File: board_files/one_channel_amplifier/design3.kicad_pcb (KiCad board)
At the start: 2 copper layers, 50.8 x 50.8 mm, 27 parts, among them J1 Screw_Terminal_01x02, J2 Screw_Terminal_01x02, J3 Screw_Terminal_01x02, J4 Conn_01x02, J5 Conn_01x02, J6 Screw_Terminal_01x02, U1 LM3886

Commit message: added 3rd design iteration
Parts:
- moved C4 55.4 mm to (119.6, 88.4), turned to 90 degrees
- moved J3 53.9 mm to (107.4, 80.8), turned to 180 degrees
- moved J2 41.5 mm to (107.4, 93.0), turned to 180 degrees
- moved J6 30.7 mm to (143.0, 106.9), turned to 0 degrees
- moved J1 30.0 mm to (107.4, 105.2), turned to 180 degrees
- moved C12 28.6 mm to (163.1, 92.2)
- moved R7 28.6 mm to (166.1, 92.2)
- moved C5 25.4 mm to (133.1, 84.1), turned to 90 degrees
- moved C10 24.7 mm to (166.4, 96.3)
- moved R4 24.7 mm to (170.9, 96.3)
- moved R5 24.7 mm to (163.3, 96.3)
- moved L1 20.1 mm to (142.5, 98.6), turned to 270 degrees
- moved C1 19.4 mm to (119.6, 105.2), turned to 90 degrees
- moved R3 17.8 mm to (146.3, 98.3), turned to 270 degrees
- moved C3 12.1 mm to (140.2, 87.1), turned to 90 degrees
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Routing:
- net GND: track 38.0 -> 0.00 mm, vias 2 -> 0
- net Net-(C10-Pad1): track 9.37 -> 0.00 mm
- net Net-(L1-Pad1): track 8.69 -> 0.00 mm, vias 16 -> 0
- net Net-(C11-Pad1): track 1.78 -> 0.00 mm
- net Net-(C12-Pad1): track 1.47 -> 0.00 mm
- net Net-(C10-Pad2): track 1.47 -> 0.00 mm
- net Net-(J6-Pad1): vias 18 -> 0
- removed copper zone on B.Cu, net Net-(J6-Pad1)
- removed copper zone on F.Cu, net Net-(J6-Pad1)
- removed copper zone on B.Cu, net Net-(L1-Pad1)
- removed copper zone on F.Cu, net Net-(L1-Pad1)
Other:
- board size 50.8 x 50.8 mm -> 78.7 x 35.6 mm

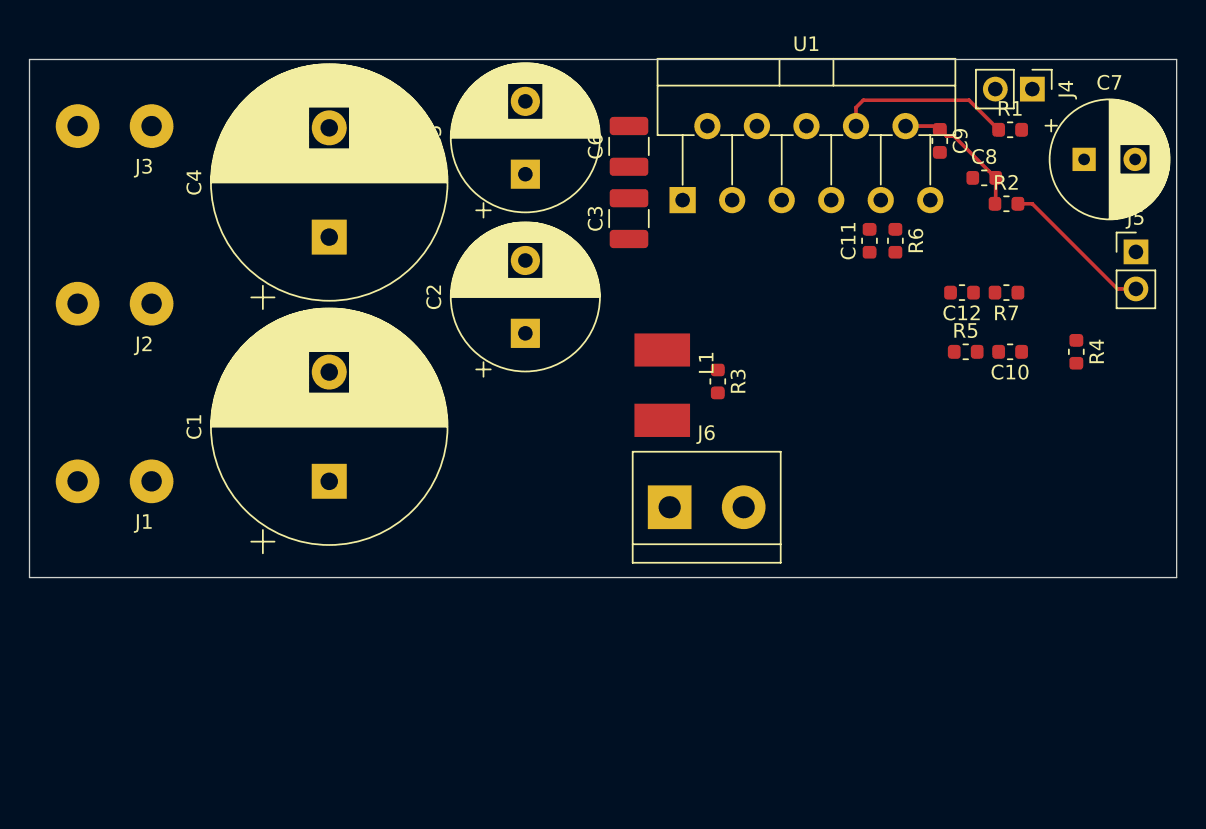
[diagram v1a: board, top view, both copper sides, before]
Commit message: added power planes
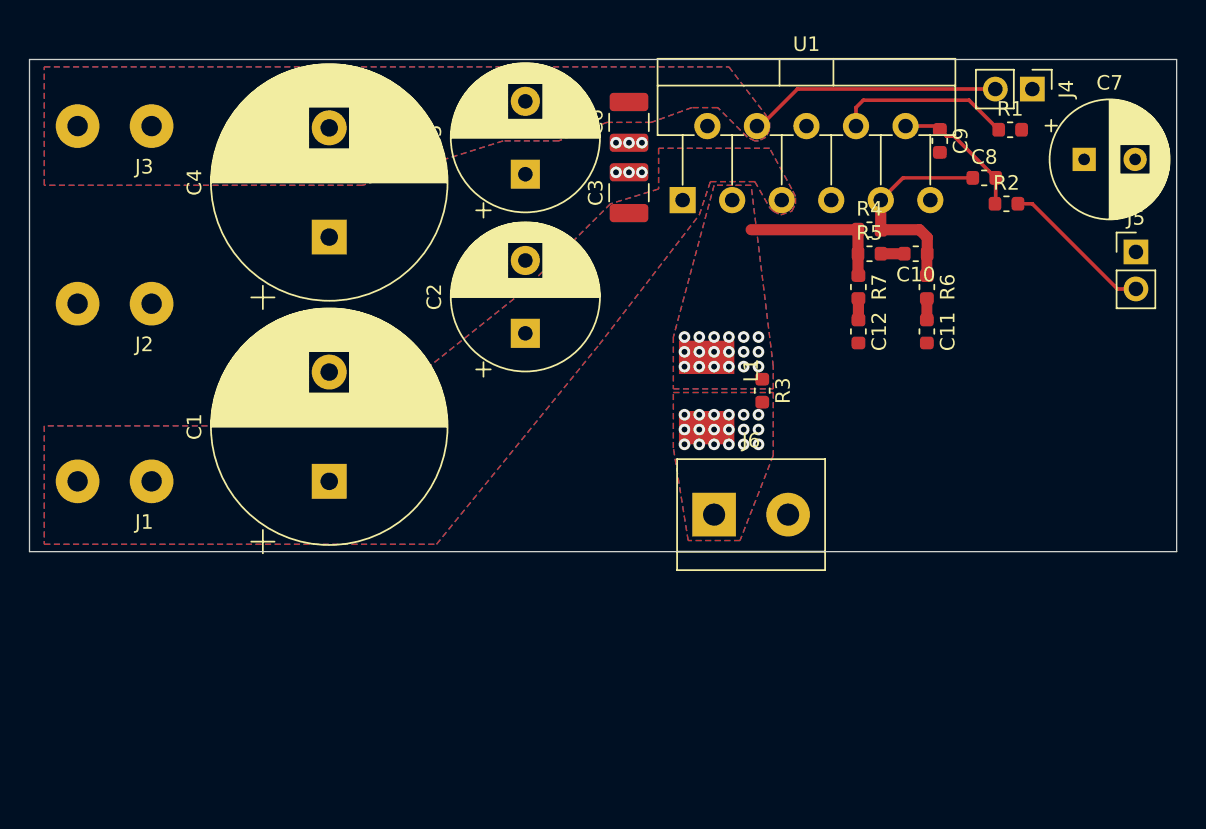
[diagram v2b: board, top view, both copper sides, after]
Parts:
- moved R4 16.5 mm to (156.7, 87.9), turned to 0 degrees
- moved R7 10.2 mm to (156.0, 91.8), turned to 270 degrees
- moved R5 9.43 mm to (156.7, 89.5)
- moved C10 9.34 mm to (159.9, 89.5)
- moved C12 7.60 mm to (156.0, 94.9), turned to 270 degrees
- moved C11 7.36 mm to (160.7, 94.9), turned to 270 degrees
- moved R6 3.84 mm to (160.7, 91.8)
- moved R3 3.11 mm to (149.4, 98.9)
- moved J6 3.09 mm to (146.1, 107.4)
- moved L1 3.09 mm to (145.5, 99.1)
- moved C3 1.78 mm to (140.2, 85.3)
- moved C6 1.65 mm to (140.2, 80.5)
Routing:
- net VEE: track 0.00 -> 17.4 mm
- net Net-(C10-Pad1): track 0.00 -> 15.0 mm
- net Net-(L1-Pad1): track 0.00 -> 10.5 mm, vias 0 -> 18
- net Net-(C10-Pad2): track 0.00 -> 1.60 mm
- net Net-(C12-Pad1): track 0.00 -> 1.47 mm
- net Net-(C11-Pad1): track 0.00 -> 1.47 mm
- net Net-(J6-Pad1): vias 0 -> 18
- net GND: vias 0 -> 6
- added copper zone on B.Cu, net Net-(J6-Pad1)
- added copper zone on F.Cu, net Net-(J6-Pad1)
- added copper zone on B.Cu, net Net-(L1-Pad1)
- added copper zone on F.Cu, net Net-(L1-Pad1)
- added copper zone on B.Cu, net VCC
- added copper zone on F.Cu, net VCC
- added copper zone on B.Cu, net VEE
- added copper zone on F.Cu, net VEE
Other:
- board size 78.7 x 35.6 mm -> 78.7 x 33.8 mm
